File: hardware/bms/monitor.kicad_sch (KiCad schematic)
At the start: 113 parts, among them Q2 Q_PMOS_GSD, Q3 Q_PMOS_GSD, U1 BQ76952

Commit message: Added Micro SD card circuit.
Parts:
- removed C20, C23: 0.1uF, Capacitor_SMD:C_0805_2012Metric, symbol Device:C_Small
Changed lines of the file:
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@@
   (junction (at 123.19 232.41) (diameter 0) (color 0 0 0 0)
-  )
-  (junction (at 44.45 74.93) (diameter 0) (color 0 0 0 0)
   )
   (junction (at 212.09 101.6) (diameter 0) (color 0 0 0 0)
@@
     (stroke (width 0) (type default))
   )
-  (wire (pts (xy 44.45 95.25) (xy 44.45 99.06))
-    (stroke (width 0) (type default))
-  )
   (wire (pts (xy 143.51 232.41) (xy 133.35 232.41))
     (stroke (width 0) (type default))
@@
     (stroke (width 0) (type default))
   )
-  (wire (pts (xy 44.45 74.93) (xy 119.38 74.93))
-    (stroke (width 0) (type default))
-  )
   (wire (pts (xy 114.3 199.39) (xy 123.19 199.39))
     (stroke (width 0) (type default))
@@
     (stroke (width 0) (type default))
   )
-  (wire (pts (xy 44.45 74.93) (xy 44.45 80.01))
-    (stroke (width 0) (type default))
-  )
   (wire (pts (xy 168.91 236.22) (xy 168.91 243.84))
     (stroke (width 0) (type default))
@@
     (stroke (width 0) (type default))
   )
-  (wire (pts (xy 40.64 74.93) (xy 44.45 74.93))
+  (wire (pts (xy 40.64 74.93) (xy 119.38 74.93))
     (stroke (width 0) (type default))
   )
@@
   )
   (wire (pts (xy 224.79 46.99) (xy 232.41 46.99))
-    (stroke (width 0) (type default))
-  )
-  (wire (pts (xy 44.45 85.09) (xy 44.45 90.17))
     (stroke (width 0) (type default))
   )
@@
     )
   )
-  (symbol (lib_id "power:GND") (at 44.45 99.06 0) (unit 1)
-    (in_bom yes) (on_board yes) (dnp no)
-    (property "Reference" "#PWR080" (at 44.45 105.41 0)
-      (effects (font (size 1.27 1.27)) hide)
-    )
-    (property "Value" "GND" (at 44.45 102.87 0)
-      (effects (font (size 1.27 1.27)))
-    )
-    (property "Footprint" "" (at 44.45 99.06 0)
-      (effects (font (size 1.27 1.27)) hide)
-    )
-    (property "Datasheet" "" (at 44.45 99.06 0)
-      (effects (font (size 1.27 1.27)) hide)
-    )
-    (pin "1")
-    (instances
-      (project "bms"
-        (path "/a4805e9d-b940-444e-a7cb-db4f4c53ed46/00000000-0000-0000-0000-00006523a805"
-          (reference "#PWR080") (unit 1)
-        )
-      )
-    )
-  )
   (symbol (lib_id "Graphic:SYM_Arrow_Large") (at 142.24 59.69 0) (unit 1)
     (in_bom yes) (on_board yes) (dnp no)
@@
         )
       )
-    )
-  )
-  (symbol (lib_id "Device:C_Small") (at 44.45 92.71 180) (unit 1)
-    (in_bom yes) (on_board yes) (dnp no)
-    (property "Reference" "C23" (at 42.1132 95.0214 0)
-      (effects (font (size 1.27 1.27)) (justify left))
-    )
-    (property "Value" "0.1uF" (at 42.1132 92.71 0)
-      (effects (font (size 1.27 1.27)) (justify left))
-    )
-    (property "Footprint" "Capacitor_SMD:C_0805_2012Metric" (at 44.45 92.71 0)
-      (effects (font (size 1.27 1.27)) hide)
-    )
-    (property "Datasheet" "~" (at 44.45 92.71 0)
-      (effects (font (size 1.27 1.27)) hide)
-    )
-    (property "MFG" "TDK Corporation" (at 44.45 92.71 0)
-      (effects (font (size 1.27 1.27)) hide)
-    )
-    (property "MFG PN" "CGA4J3X7T2E104K125AA" (at 44.45 92.71 0)
-      (effects (font (size 1.27 1.27)) hide)
-    )
-    (property "Voltage" "250V" (at 42.1132 90.3986 0)
-      (effects (font (size 1.27 1.27)) (justify left))
-    )
-    (pin "1")
-    (pin "2")
-    (instances
-      (project "bms"
-        (path "/a4805e9d-b940-444e-a7cb-db4f4c53ed46/00000000-0000-0000-0000-00006523a805"
-          (reference "C23") (unit 1)
-        )
-      )
-    )
-  )
-  (symbol (lib_id "Device:C_Small") (at 44.45 82.55 180) (unit 1)
-    (in_bom yes) (on_board yes) (dnp no)
-    (property "Reference" "C20" (at 42.1132 84.8614 0)
-      (effects (font (size 1.27 1.27)) (justify left))
-    )
-    (property "Value" "0.1uF" (at 42.1132 82.55 0)
-      (effects (font (size 1.27 1.27)) (justify left))
-    )
-    (property "Footprint" "Capacitor_SMD:C_0805_2012Metric" (at 44.45 82.55 0)
-      (effects (font (size 1.27 1.27)) hide)
-    )
-    (property "Datasheet" "~" (at 44.45 82.55 0)
-      (effects (font (size 1.27 1.27)) hide)
-    )
-    (property "MFG" "TDK Corporation" (at 44.45 82.55 0)
-      (effects (font (size 1.27 1.27)) hide)
-    )
-    (property "MFG PN" "CGA4J3X7T2E104K125AA" (at 44.45 82.55 0)
-      (effects (font (size 1.27 1.27)) hide)
-    )
-    (property "Voltage" "250V" (at 42.1132 80.2386 0)
-      (effects (font (size 1.27 1.27)) (justify left))
-    )
-    (pin "1")
-    (pin "2")
-    (instances
-      (project "bms"
-        (path "/a4805e9d-b940-444e-a7cb-db4f4c53ed46/00000000-0000-0000-0000-00006523a805"
-          (reference "C20") (unit 1)
-        )
-      )

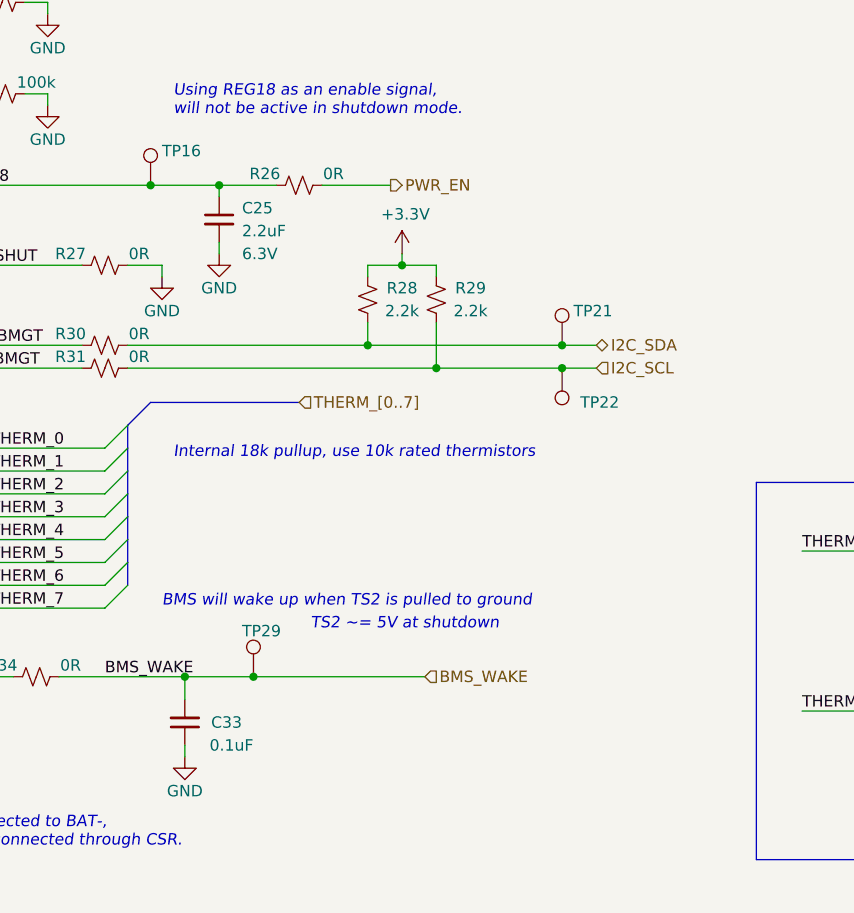
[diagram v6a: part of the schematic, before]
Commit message: Added extra features to try and prevent SD card data corruption. Added override enable so that the MCU can keep itself on until the SD card is finished writing, also added 5V / wake detect circuit so the MCU can begin to sense when the 5V rail is dropping and react accordingly
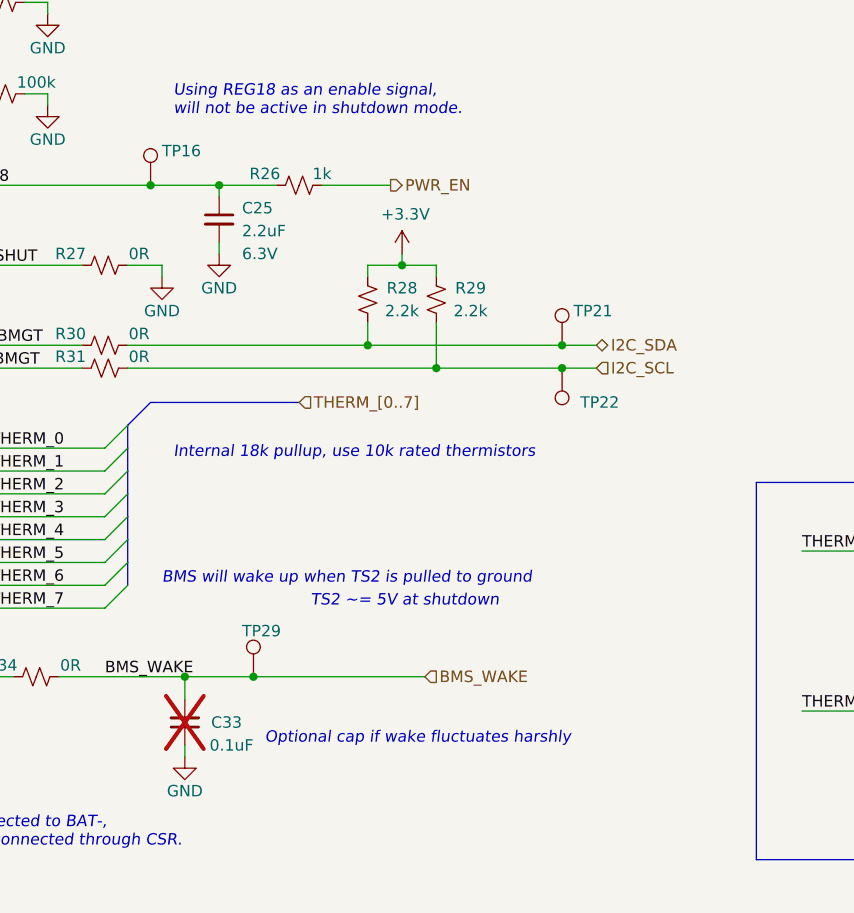
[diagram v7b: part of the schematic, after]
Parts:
- C33: now not fitted
- R26: value 0R -> 1k; MFG PN ERJ-3GEY0R00V -> ERJ-3EKF1001V; Power (none) -> 1/10W
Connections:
- net PWR_EN: now also R26.1; no longer R26.2
- net REG18: now also R26.2; no longer R26.1
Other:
- note added: "Optional cap if wake fluctuates harshly"
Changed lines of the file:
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@@
     (effects (font (size 1.27 1.27) italic) (justify left bottom))
   )
-  (text "TS2 ~= 5V at shutdown" (at 251.46 196.85 0)
+  (text "TS2 ~= 5V at shutdown" (at 251.46 194.31 0)
     (effects (font (size 1.27 1.27) italic) (justify left bottom))
   )
@@
     (effects (font (size 1.27 1.27)) (justify left bottom))
   )
-  (text "BMS will wake up when TS2 is pulled to ground" (at 234.95 194.31 0)
+  (text "BMS will wake up when TS2 is pulled to ground" (at 234.95 191.77 0)
     (effects (font (size 1.27 1.27) italic) (justify left bottom))
   )
@@
     (effects (font (size 1.27 1.27) italic) (justify left bottom))
   )
+  (text "Optional cap if wake fluctuates harshly" (at 246.38 209.55 0)
+    (effects (font (size 1.27 1.27) italic) (justify left bottom))
+  )
   (text "Discharge" (at 55.88 78.74 0)
     (effects (font (size 1.27 1.27) italic) (justify left bottom))
@@
     )
   )
-  (symbol (lib_id "Device:R_Small_US") (at 250.19 147.32 90) (unit 1)
-    (in_bom yes) (on_board yes) (dnp no)
-    (property "Reference" "R26" (at 246.38 146.05 90)
-      (effects (font (size 1.27 1.27)))
-    )
-    (property "Value" "0R" (at 254 146.05 90)
-      (effects (font (size 1.27 1.27)))
-    )
-    (property "Footprint" "Resistor_SMD:R_0603_1608Metric" (at 250.19 147.32 0)
-      (effects (font (size 1.27 1.27)) hide)
-    )
-    (property "Datasheet" "~" (at 250.19 147.32 0)
-      (effects (font (size 1.27 1.27)) hide)
-    )
-    (property "MFG" "Panasonic Electronic Components" (at 250.19 147.32 90)
-      (effects (font (size 1.27 1.27)) hide)
-    )
-    (property "MFG PN" "ERJ-3GEY0R00V" (at 250.19 147.32 90)
-      (effects (font (size 1.27 1.27)) hide)
-    )
-    (pin "1")
-    (pin "2")
-    (instances
-      (project "bms"
-        (path "/a4805e9d-b940-444e-a7cb-db4f4c53ed46/00000000-0000-0000-0000-00006523a805"
-          (reference "R26") (unit 1)
-        )
-      )
-    )
-  )
   (symbol (lib_id "Device:C_Small") (at 241.3 151.13 0) (unit 1)
     (in_bom yes) (on_board yes) (dnp no)
@@
   )
   (symbol (lib_id "Device:C_Small") (at 237.49 207.01 180) (unit 1)
-    (in_bom yes) (on_board yes) (dnp no)
+    (in_bom yes) (on_board yes) (dnp yes)
     (property "Reference" "C33" (at 243.84 207.01 0)
       (effects (font (size 1.27 1.27)) (justify left))
@@
         )
       )
+    )
+  )
+  (symbol (lib_id "Device:R_Small_US") (at 250.19 147.32 270) (unit 1)
+    (in_bom yes) (on_board yes) (dnp no)
+    (property "Reference" "R26" (at 246.38 146.05 90)
+      (effects (font (size 1.27 1.27)))
+    )
+    (property "Value" "1k" (at 252.73 146.05 90)
+      (effects (font (size 1.27 1.27)))
+    )
+    (property "Footprint" "Resistor_SMD:R_0603_1608Metric" (at 250.19 147.32 0)
+      (effects (font (size 1.27 1.27)) hide)
+    )
+    (property "Datasheet" "~" (at 250.19 147.32 0)
+      (effects (font (size 1.27 1.27)) hide)
+    )
+    (property "MFG" "Panasonic Electronic Components" (at 250.19 147.32 90)
+      (effects (font (size 1.27 1.27)) hide)
+    )
+    (property "MFG PN" "ERJ-3EKF1001V" (at 250.19 147.32 90)
+      (effects (font (size 1.27 1.27)) hide)
+    )
+    (property "Power" "1/10W" (at 250.19 147.32 0)
+      (effects (font (size 1.27 1.27)) hide)
+    )
+    (pin "1")
+    (pin "2")
+    (instances
+      (project "bms"
+        (path "/a4805e9d-b940-444e-a7cb-db4f4c53ed46/00000000-0000-0000-0000-00006523a805"
+          (reference "R26") (unit 1)
+        )
+        (path "/a4805e9d-b940-444e-a7cb-db4f4c53ed46/00000000-0000-0000-0000-00006523ab32"
+          (reference "R?") (unit 1)
+        )
+        (path "/a4805e9d-b940-444e-a7cb-db4f4c53ed46/00000000-0000-0000-0000-00006658c265"
+          (reference "R?") (unit 1)
+        )
+      )

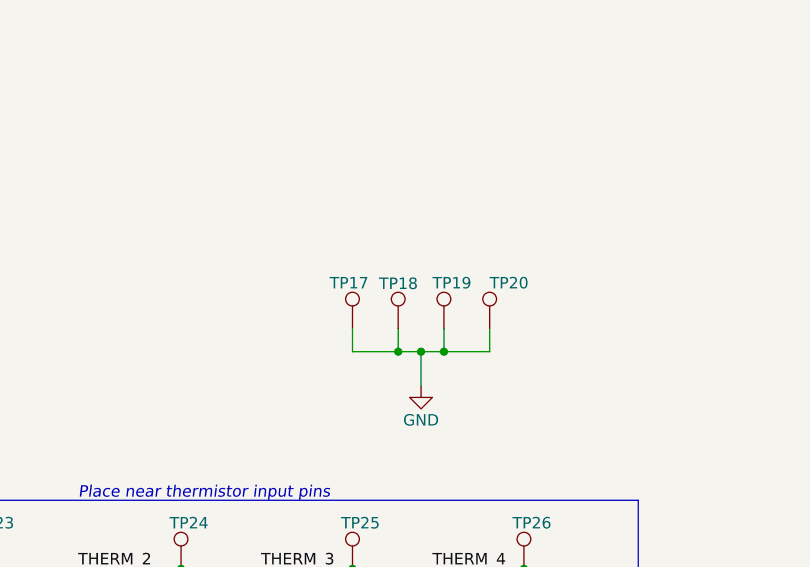
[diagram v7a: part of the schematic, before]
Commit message: Added keystone clip test points for ground, should be nice
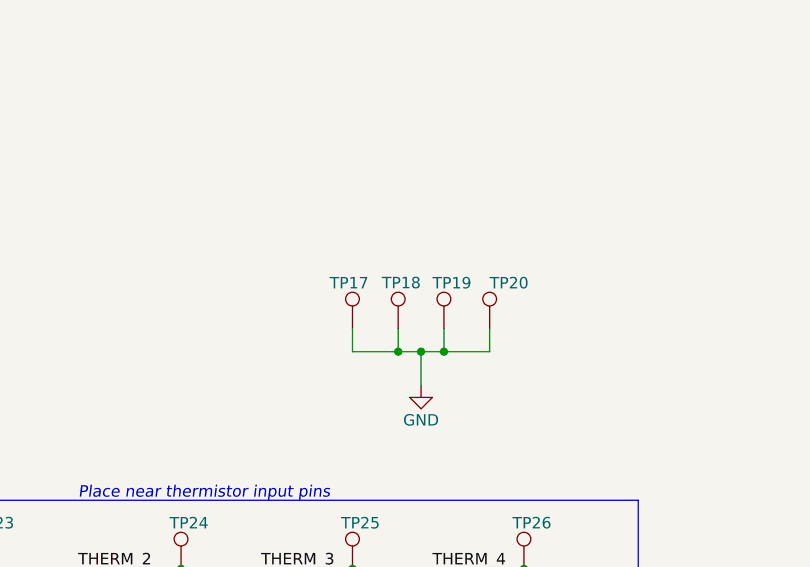
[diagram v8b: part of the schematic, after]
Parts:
- TP17, TP18: footprint bms:TestPoint_Pad_D0.5mm -> bms:TestPoint_Keystone_5019_Minature; MFG (none) -> Keystone Electronics; MFG PN (none) -> 5019; now in the parts list
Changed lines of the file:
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@@
+    )
+  )
+  (symbol (lib_id "Connector:TestPoint") (at 375.92 205.74 0) (unit 1)
+    (in_bom no) (on_board yes) (dnp no)
+    (property "Reference" "TP33" (at 372.11 200.66 0)
+      (effects (font (size 1.27 1.27)) (justify left))
+    )
+    (property "Value" "TestPoint" (at 377.3932 205.0542 0)
+      (effects (font (size 1.27 1.27)) (justify left) hide)
+    )
+    (property "Footprint" "bms:TestPoint_Pad_D0.5mm" (at 381 205.74 0)
+      (effects (font (size 1.27 1.27)) hide)
+    )
+    (property "Datasheet" "~" (at 381 205.74 0)
+      (effects (font (size 1.27 1.27)) hide)
+    )
+    (pin "1")
+    (instances
+      (project "bms"
+        (path "/a4805e9d-b940-444e-a7cb-db4f4c53ed46/00000000-0000-0000-0000-00006523a805"
+          (reference "TP33") (unit 1)
+        )
+        (path "/a4805e9d-b940-444e-a7cb-db4f4c53ed46/00000000-0000-0000-0000-00006523ab32"
+          (reference "TP?") (unit 1)
+        )
+      )
     )
   )
   (symbol (lib_id "Connector:TestPoint") (at 361.95 161.29 0) (unit 1)
-    (in_bom no) (on_board yes) (dnp no)
-    (property "Reference" "TP18" (at 359.8153 156.2748 0)
+    (in_bom yes) (on_board yes) (dnp no)
+    (property "Reference" "TP18" (at 360.1324 156.1935 0)
       (effects (font (size 1.27 1.27)) (justify left))
     )
@@
       (effects (font (size 1.27 1.27)) (justify left) hide)
     )
-    (property "Footprint" "bms:TestPoint_Pad_D0.5mm" (at 367.03 161.29 0)
+    (property "Footprint" "bms:TestPoint_Keystone_5019_Minature" (at 367.03 161.29 0)
       (effects (font (size 1.27 1.27)) hide)
     )
@@
       (effects (font (size 1.27 1.27)) hide)
     )
+    (property "MFG" "Keystone Electronics" (at 361.95 161.29 0)
+      (effects (font (size 1.27 1.27)) hide)
+    )
+    (property "MFG PN" "5019" (at 361.95 161.29 0)
+      (effects (font (size 1.27 1.27)) hide)
+    )
     (pin "1")
     (instances
@@
         (path "/a4805e9d-b940-444e-a7cb-db4f4c53ed46/00000000-0000-0000-0000-00006523a805"
           (reference "TP18") (unit 1)
-        )
-        (path "/a4805e9d-b940-444e-a7cb-db4f4c53ed46/00000000-0000-0000-0000-00006523ab32"
-          (reference "TP?") (unit 1)
-        )
-      )
-    )
-  )
-  (symbol (lib_id "Connector:TestPoint") (at 375.92 205.74 0) (unit 1)
-    (in_bom no) (on_board yes) (dnp no)
-    (property "Reference" "TP33" (at 372.11 200.66 0)
-      (effects (font (size 1.27 1.27)) (justify left))
-    )
-    (property "Value" "TestPoint" (at 377.3932 205.0542 0)
-      (effects (font (size 1.27 1.27)) (justify left) hide)
-    )
-    (property "Footprint" "bms:TestPoint_Pad_D0.5mm" (at 381 205.74 0)
-      (effects (font (size 1.27 1.27)) hide)
-    )
-    (property "Datasheet" "~" (at 381 205.74 0)
-      (effects (font (size 1.27 1.27)) hide)
-    )
-    (pin "1")
-    (instances
-      (project "bms"
-        (path "/a4805e9d-b940-444e-a7cb-db4f4c53ed46/00000000-0000-0000-0000-00006523a805"
-          (reference "TP33") (unit 1)
         )
         (path "/a4805e9d-b940-444e-a7cb-db4f4c53ed46/00000000-0000-0000-0000-00006523ab32"
@@
   )
   (symbol (lib_id "Connector:TestPoint") (at 356.87 161.29 0) (unit 1)
-    (in_bom no) (on_board yes) (dnp no)
+    (in_bom yes) (on_board yes) (dnp no)
     (property "Reference" "TP17" (at 354.33 156.21 0)
       (effects (font (size 1.27 1.27)) (justify left))
@@
       (effects (font (size 1.27 1.27)) (justify left) hide)
     )
-    (property "Footprint" "bms:TestPoint_Pad_D0.5mm" (at 361.95 161.29 0)
+    (property "Footprint" "bms:TestPoint_Keystone_5019_Minature" (at 361.95 161.29 0)
       (effects (font (size 1.27 1.27)) hide)
     )
@@
       (effects (font (size 1.27 1.27)) hide)
     )
+    (property "MFG" "Keystone Electronics" (at 356.87 161.29 0)
+      (effects (font (size 1.27 1.27)) hide)
+    )
+    (property "MFG PN" "5019" (at 356.87 161.29 0)
+      (effects (font (size 1.27 1.27)) hide)
+    )
